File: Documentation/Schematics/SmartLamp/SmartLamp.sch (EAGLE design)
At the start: 34 parts, among them J1 POWER_JACKPTH_BREAD, Q1 STN4NF03L, Q2 STN4NF03L, Q3 STN4NF03L, U2 DS3231MZ, U3 ATMEGA8/168/328, U4 HM-10, X1 16MHz

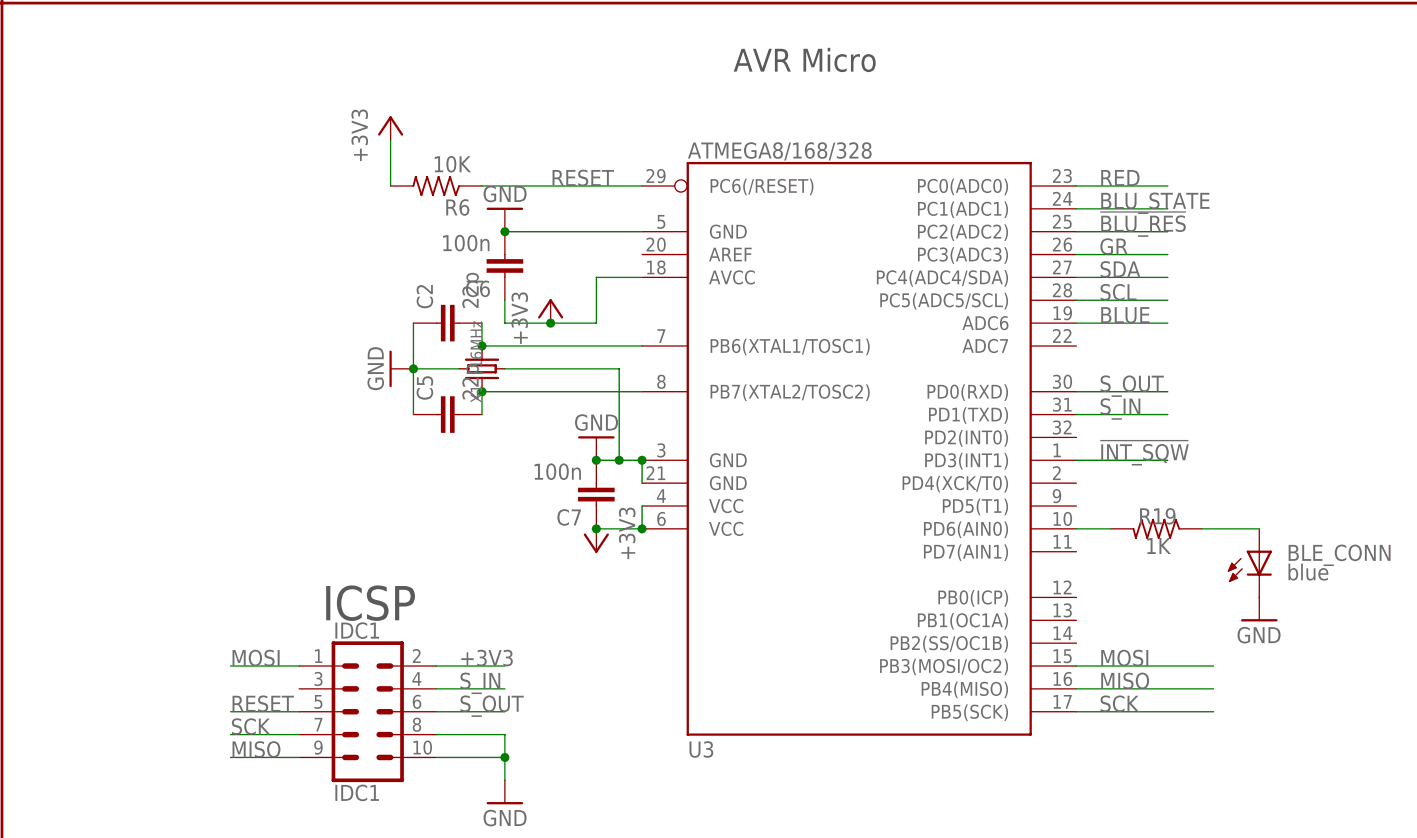
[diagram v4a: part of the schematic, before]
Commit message: Changed pinout for atmega.
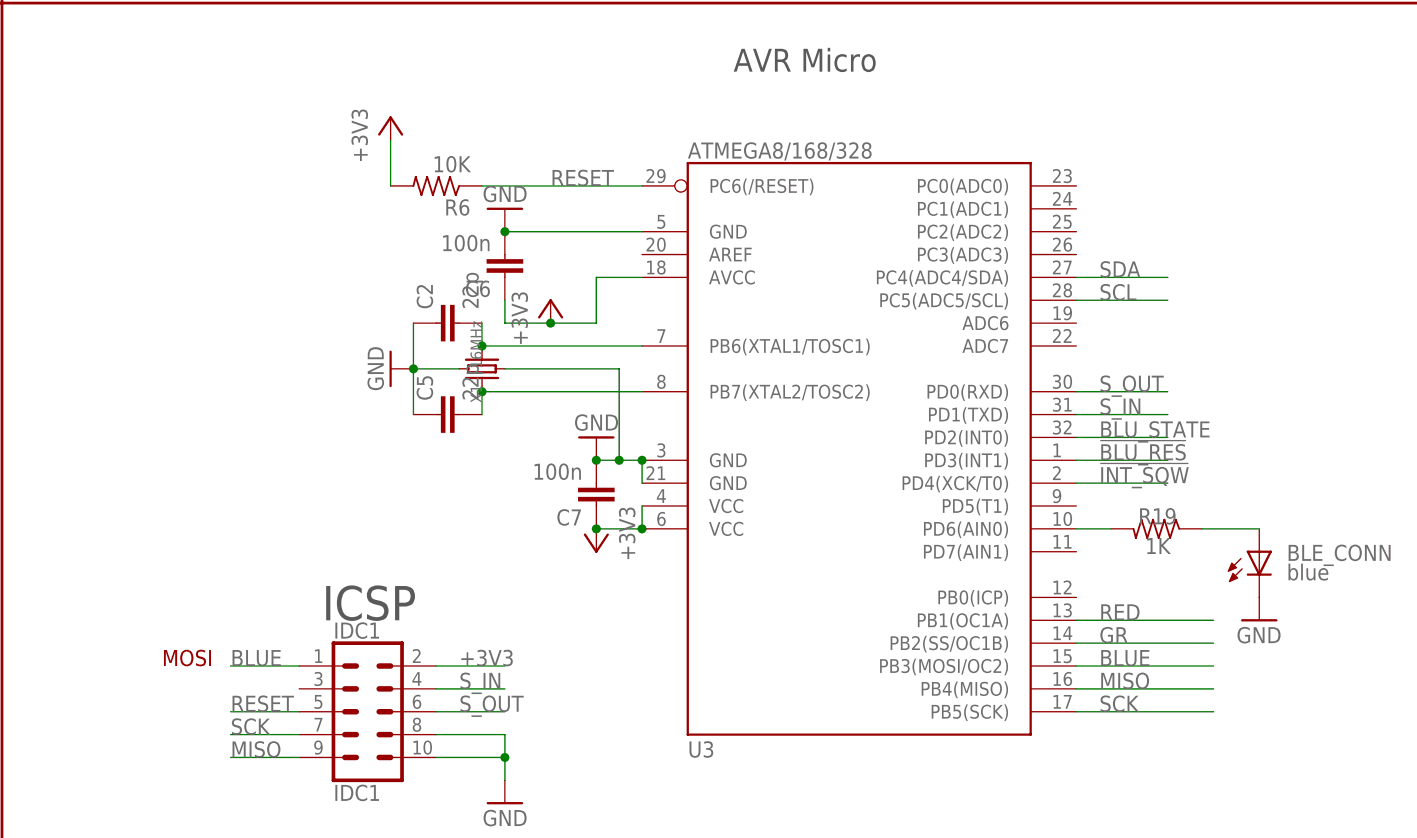
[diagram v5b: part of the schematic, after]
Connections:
- removed net MOSI: IDC1.1, U3.PB3(MOSI/OC2)
- net !BLU_RES: no longer U3.PC2(ADC2)
- net !INT_SQW: now also U3.PD4(XCK/T0); no longer U3.PD3(INT1)
- net BLUE: now also IDC1.1, U3.PB3(MOSI/OC2); no longer U3.ADC6
- net BLU_STATE: no longer U3.PC1(ADC1)
- net GR: now also U3.PB2(SS/OC1B); no longer U3.PC3(ADC3)
- net RED: now also U3.PB1(OC1A); no longer U3.PC0(ADC0)
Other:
- note added: "MOSI"
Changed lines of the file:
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@@
 <text x="157.48" y="81.28" size="2.54" layer="97" font="vector" ratio="16">Bluetooth module</text>
 <wire x1="256.54" y1="86.36" x2="256.54" y2="5.08" width="0.3048" layer="94"/>
+<text x="274.32" y="109.22" size="1.778" layer="94" font="vector">MOSI</text>
 </plain>
 <instances>
@@
 </segment>
 <segment>
-<pinref part="U3" gate="G$1" pin="PD3(INT1)"/>
-<wire x1="375.92" y1="132.08" x2="386.08" y2="132.08" width="0.1524" layer="91"/>
-<label x="378.46" y="132.08" size="1.778" layer="95" font="vector"/>
+<pinref part="U3" gate="G$1" pin="PD4(XCK/T0)"/>
+<wire x1="375.92" y1="129.54" x2="386.08" y2="129.54" width="0.1524" layer="91"/>
+<label x="378.46" y="129.54" size="1.778" layer="95" font="vector"/>
 </segment>
 </net>
@@
 </segment>
 <segment>
-<pinref part="U3" gate="G$1" pin="PC1(ADC1)"/>
-<wire x1="375.92" y1="160.02" x2="386.08" y2="160.02" width="0.1524" layer="91"/>
-<label x="378.46" y="160.02" size="1.778" layer="95" font="vector"/>
+<wire x1="375.92" y1="134.62" x2="386.08" y2="134.62" width="0.1524" layer="91"/>
+<label x="378.46" y="134.62" size="1.778" layer="95" font="vector"/>
 </segment>
 </net>
@@
 </segment>
 <segment>
-<pinref part="U3" gate="G$1" pin="PC3(ADC3)"/>
-<wire x1="375.92" y1="154.94" x2="386.08" y2="154.94" width="0.1524" layer="91"/>
-<label x="378.46" y="154.94" size="1.778" layer="95" font="vector"/>
+<pinref part="U3" gate="G$1" pin="PB2(SS/OC1B)"/>
+<wire x1="375.92" y1="111.76" x2="391.16" y2="111.76" width="0.1524" layer="91"/>
+<label x="378.46" y="111.76" size="1.778" layer="95" font="vector"/>
 </segment>
 </net>
@@
 </segment>
 <segment>
-<pinref part="U3" gate="G$1" pin="ADC6"/>
-<wire x1="375.92" y1="147.32" x2="386.08" y2="147.32" width="0.1524" layer="91"/>
-<label x="378.46" y="147.32" size="1.778" layer="95" font="vector"/>
+<pinref part="U3" gate="G$1" pin="PB3(MOSI/OC2)"/>
+<wire x1="375.92" y1="109.22" x2="391.16" y2="109.22" width="0.1524" layer="91"/>
+<label x="378.46" y="109.22" size="1.778" layer="95"/>
+</segment>
+<segment>
+<pinref part="IDC1" gate="G$1" pin="1"/>
+<wire x1="289.56" y1="109.22" x2="281.94" y2="109.22" width="0.1524" layer="91"/>
+<label x="281.94" y="109.22" size="1.778" layer="95" font="vector"/>
 </segment>
 </net>
@@
 </segment>
 <segment>
-<pinref part="U3" gate="G$1" pin="PC2(ADC2)"/>
-<wire x1="375.92" y1="157.48" x2="386.08" y2="157.48" width="0.1524" layer="91"/>
-<label x="378.46" y="157.48" size="1.778" layer="95" font="vector"/>
+<wire x1="375.92" y1="132.08" x2="386.08" y2="132.08" width="0.1524" layer="91"/>
+<label x="378.46" y="132.08" size="1.778" layer="95" font="vector"/>
 </segment>
 </net>
@@
 </segment>
 <segment>
-<pinref part="U3" gate="G$1" pin="PC0(ADC0)"/>
-<wire x1="375.92" y1="162.56" x2="386.08" y2="162.56" width="0.1524" layer="91"/>
-<label x="378.46" y="162.56" size="1.778" layer="95" font="vector"/>
+<pinref part="U3" gate="G$1" pin="PB1(OC1A)"/>
+<wire x1="375.92" y1="114.3" x2="391.16" y2="114.3" width="0.1524" layer="91"/>
+<label x="378.46" y="114.3" size="1.778" layer="95" font="vector"/>
 </segment>
 </net>
@@
 </segment>
 </net>
-<net name="MOSI" class="0">
-<segment>
-<pinref part="U3" gate="G$1" pin="PB3(MOSI/OC2)"/>
-<wire x1="375.92" y1="109.22" x2="391.16" y2="109.22" width="0.1524" layer="91"/>
-<label x="378.46" y="109.22" size="1.778" layer="95"/>
-</segment>
-<segment>
-<pinref part="IDC1" gate="G$1" pin="1"/>
-<wire x1="289.56" y1="109.22" x2="281.94" y2="109.22" width="0.1524" layer="91"/>
-<label x="281.94" y="109.22" size="1.778" layer="95" font="vector"/>
-</segment>
-</net>

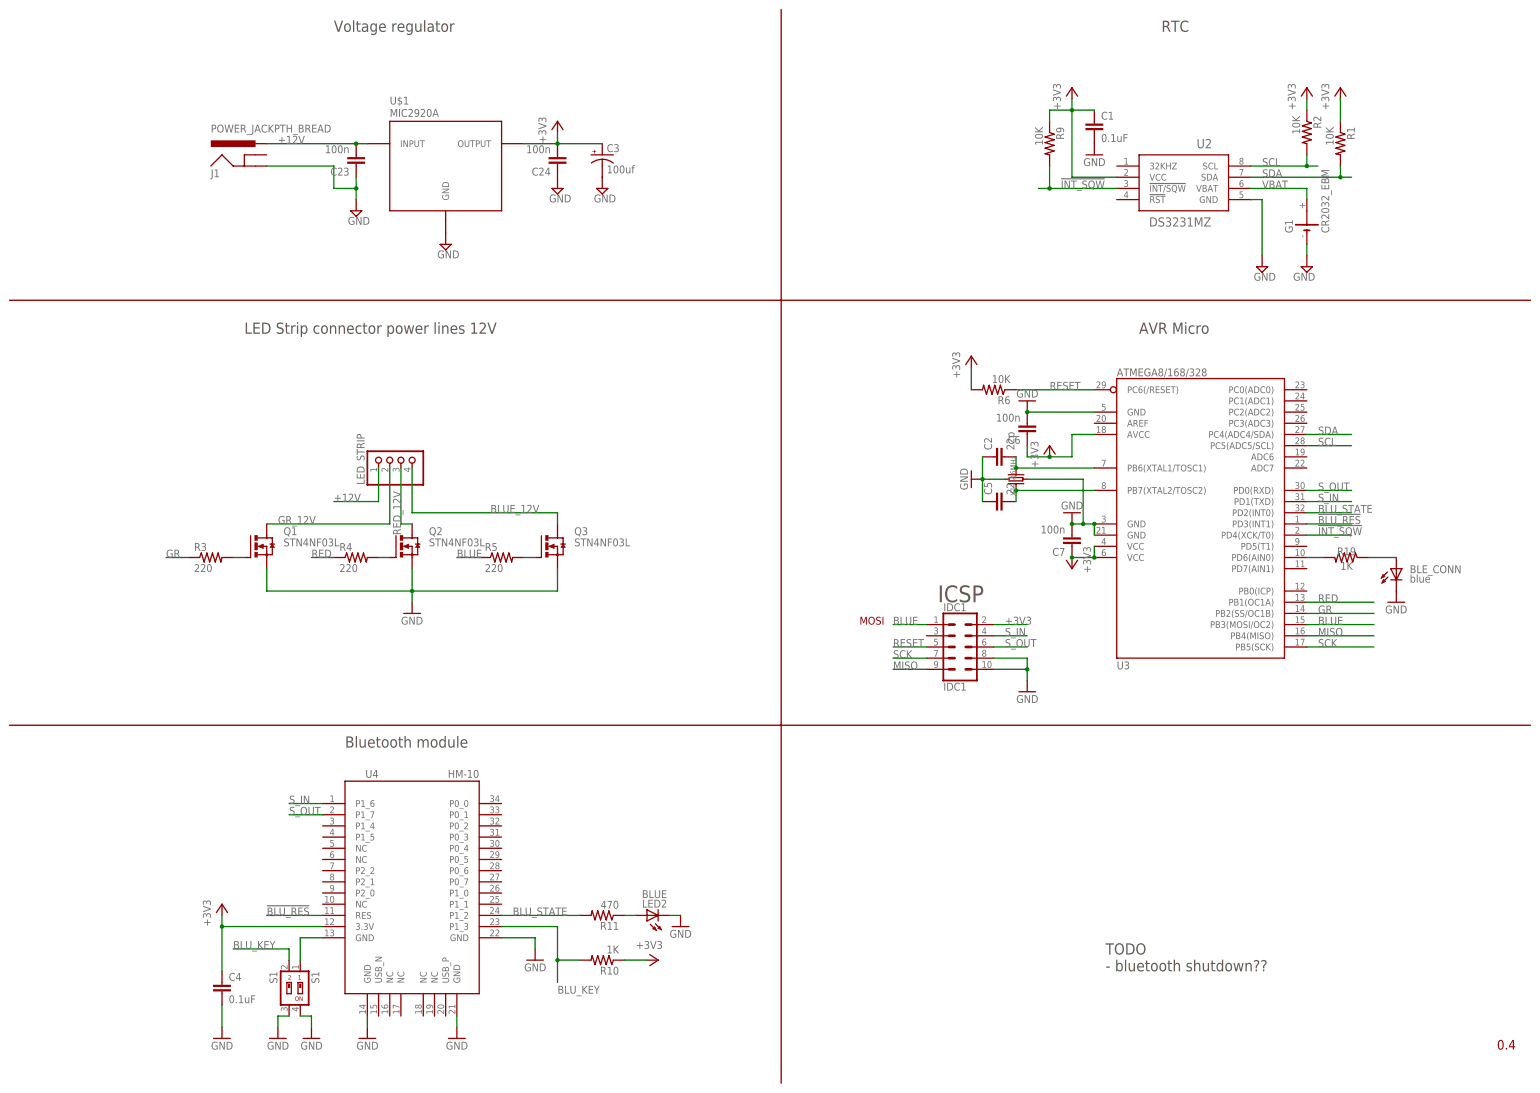
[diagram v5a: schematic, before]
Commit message: New BOM, with updated format. Fixed schematich and re-routed board
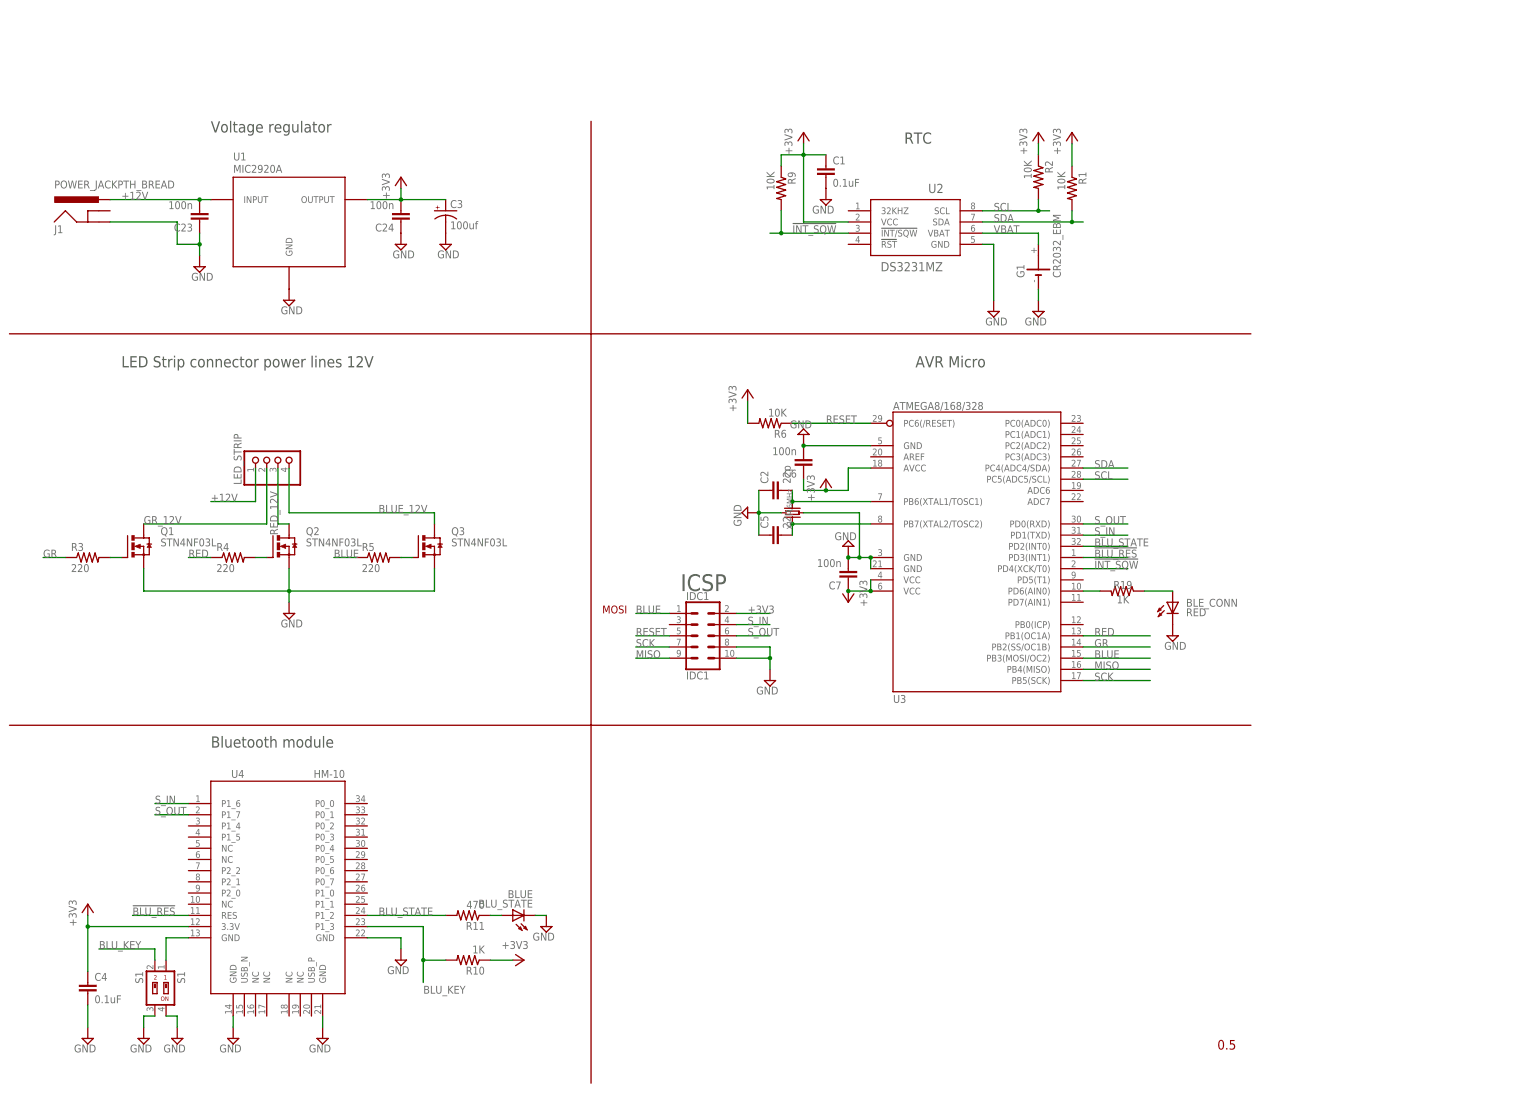
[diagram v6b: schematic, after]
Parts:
- removed LED2: BLUE, adafruit:LEDCHIP-LED0805
- removed U$1: MIC2920A, Microchip_LDO_regulator:MIC2920A
- added BLU_STATE: BLUE, adafruit:LEDCHIP-LED0805
- added U1: MIC2920A, Microchip_LDO_regulator:MIC2920A
- BLE_CONN: value blue -> RED
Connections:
- net !BLU_RES: now also U3.PD3(INT1)
- net +12V: now also U1.INPUT; no longer U$1.INPUT
- net +3V3: now also U1.OUTPUT; no longer U$1.OUTPUT
- net BLU_STATE: now also U3.PD2(INT0)
- net GND: now also BLU_STATE.C, U1.GND; no longer LED2.C, U$1.GND
- net N$1: now also BLU_STATE.A; no longer LED2.A
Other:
- note removed: "TODO - bluetooth shutdown??"
- moved on the sheet: BLE_CONN, C1, C2, C23, C24, C3, C4, C5, C6, C7, G1, IDC1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
